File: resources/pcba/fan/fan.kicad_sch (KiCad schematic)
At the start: 7 parts, among them Q1 PMOS 9301

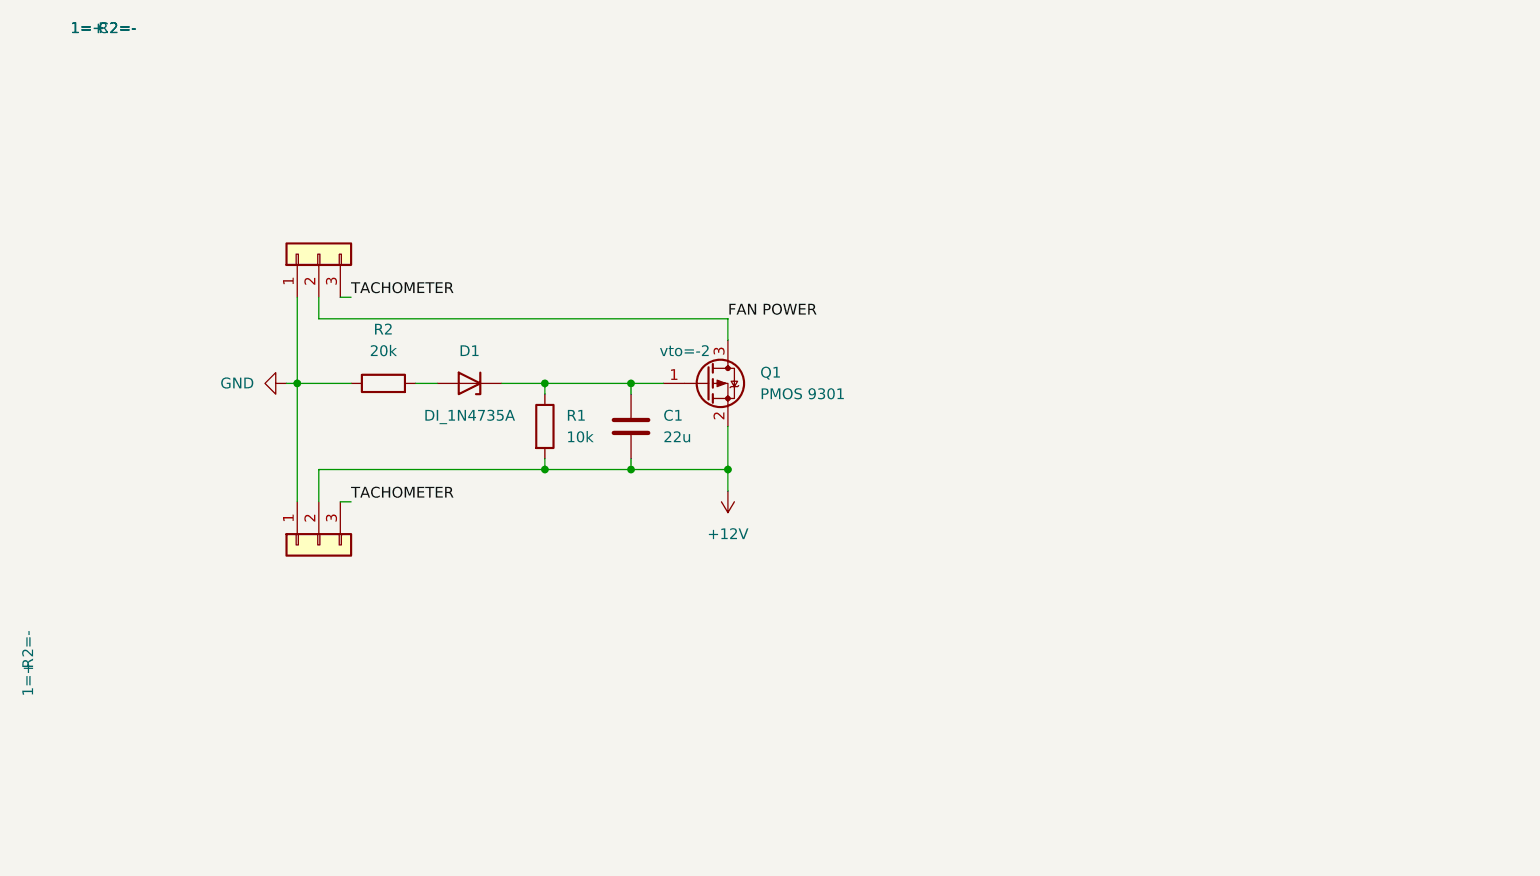
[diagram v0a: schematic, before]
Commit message: add uvp and fan pcb
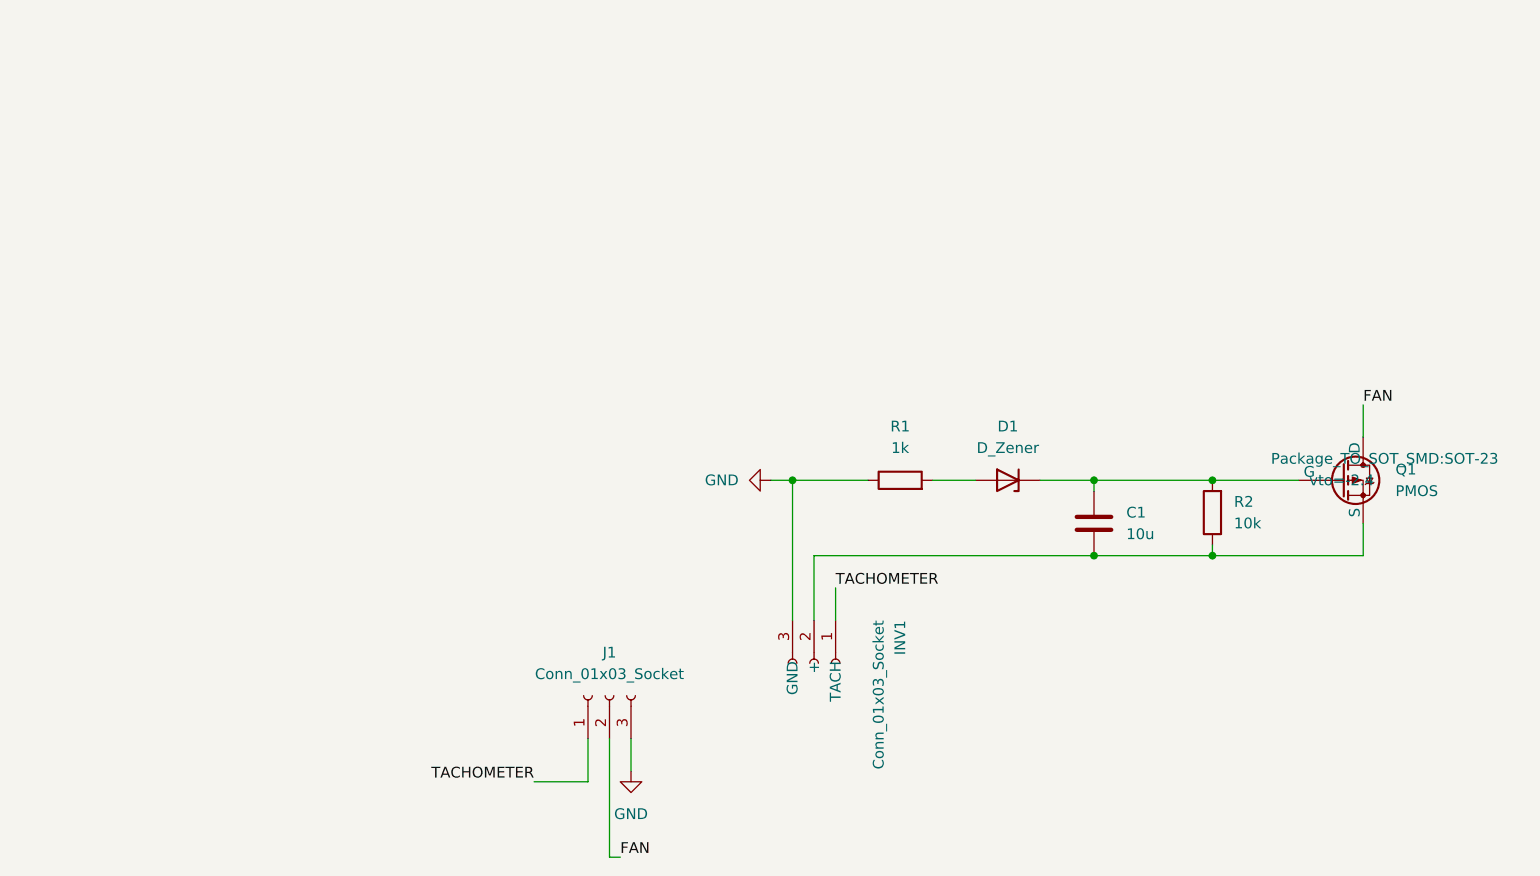
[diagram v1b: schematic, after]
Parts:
- removed IN1, IN2: ${SIM.PARAMS}, Connector_JST:JST_PH_B3B-PH-K_1x03_P2.00mm_Vertical, symbol Connector_Generic:Conn_01x03
- removed Q1: PMOS 9301, Package_TO_SOT_SMD:SOT-23, symbol Transistor_FET:IRLML9301
- added INV1: Conn_01x03_Socket, Connector_JST:JST_PH_B3B-PH-K_1x03_P2.00mm_Vertical, symbol Connector:Conn_01x03_Socket
- added J1: Conn_01x03_Socket, symbol Connector:Conn_01x03_Socket
- added Q1: PMOS, Package_TO_SOT_SMD:SOT-23, symbol Simulation_SPICE:PMOS
- C1: value 22u -> 10u
- R1: value 10k -> 1k
- R2: value 20k -> 10k
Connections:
- net GND: now also R1.1, INV1.3 (GND), J1.3 (Pin_3); no longer R2.1
- net TACHOMETER: now also INV1.1 (TACH), J1.1 (Pin_1)
- net at C1.1, D1.1 (K): now also R2.2, Q1.2 (G); no longer R1.1
- net at D1.2 (A): now also R1.2; no longer R2.2
- net +12V: no longer names the net of C1.2
- net +12V: now also R2.1, INV1.2 (+), Q1.3 (S); no longer R1.2
- new net FAN: J1.2 (Pin_2), Q1.1 (D)
